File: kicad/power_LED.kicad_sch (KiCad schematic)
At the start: 2 parts

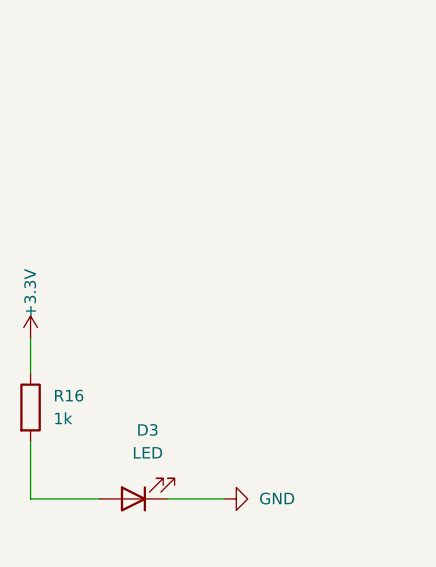
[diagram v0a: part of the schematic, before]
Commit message: feat: remake power management and use the same as the reference DK
Signed-off-by: Bobo Bäck Engström <bobo@id8-engineering.io>
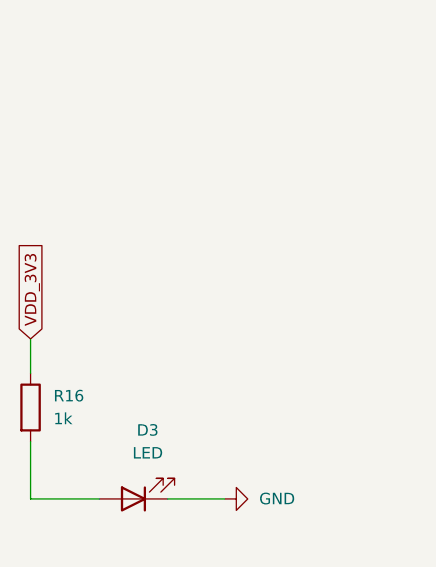
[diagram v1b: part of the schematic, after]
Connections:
- net +3.3V renamed VDD_3V3
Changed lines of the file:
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@@
 		)
 	)
-	(symbol
-		(lib_id "seven_lib:+3V3")
-		(at 87.63 87.63 0)
-		(unit 1)
-		(exclude_from_sim no)
-		(in_bom yes)
-		(on_board yes)
-		(dnp no)
-		(property "Reference" "#PWR044"
-			(at 87.63 91.44 0)
+	(global_label "VDD_3V3"
+		(shape input)
+		(at 87.63 87.63 90)
+		(fields_autoplaced yes)
+		(effects
+			(font
+				(size 1.27 1.27)
+			)
+			(justify left)
+		)
+		(property "Intersheetrefs" "${INTERSHEET_REFS}"
+			(at 87.63 76.541 90)
 			(effects
 				(font
 					(size 1.27 1.27)
 				)
+				(justify left)
 				(hide yes)
 			)
 		)
-		(property "Value" "+3.3V"
-			(at 87.63 82.55 90)
-			(effects
-				(font
-					(size 1.27 1.27)
-				)
-			)
-		)
-		(property "Footprint" ""
-			(at 87.63 87.63 0)
-			(effects
-				(font
-					(size 1.27 1.27)
-				)
-				(hide yes)
-			)
-		)
-		(property "Datasheet" ""
-			(at 87.63 87.63 0)
-			(effects
-				(font
-					(size 1.27 1.27)
-				)
-				(hide yes)
-			)
-		)
-		(property "Description" "Power symbol creates a global label with name \"+3V3\""
-			(at 87.63 87.63 0)
-			(effects
-				(font
-					(size 1.27 1.27)
-				)
-				(hide yes)
-			)
-		)
-		(pin "1"
-		)
-		(instances
-			(project "seven"
-				(path "/8e3cc843-5797-49f3-8b3a-1c11450ccd1e/184102d6-38c7-410c-9d7f-e631dd7f9fe2"
-					(reference "#PWR044")
-					(unit 1)
-				)
-			)
-		)

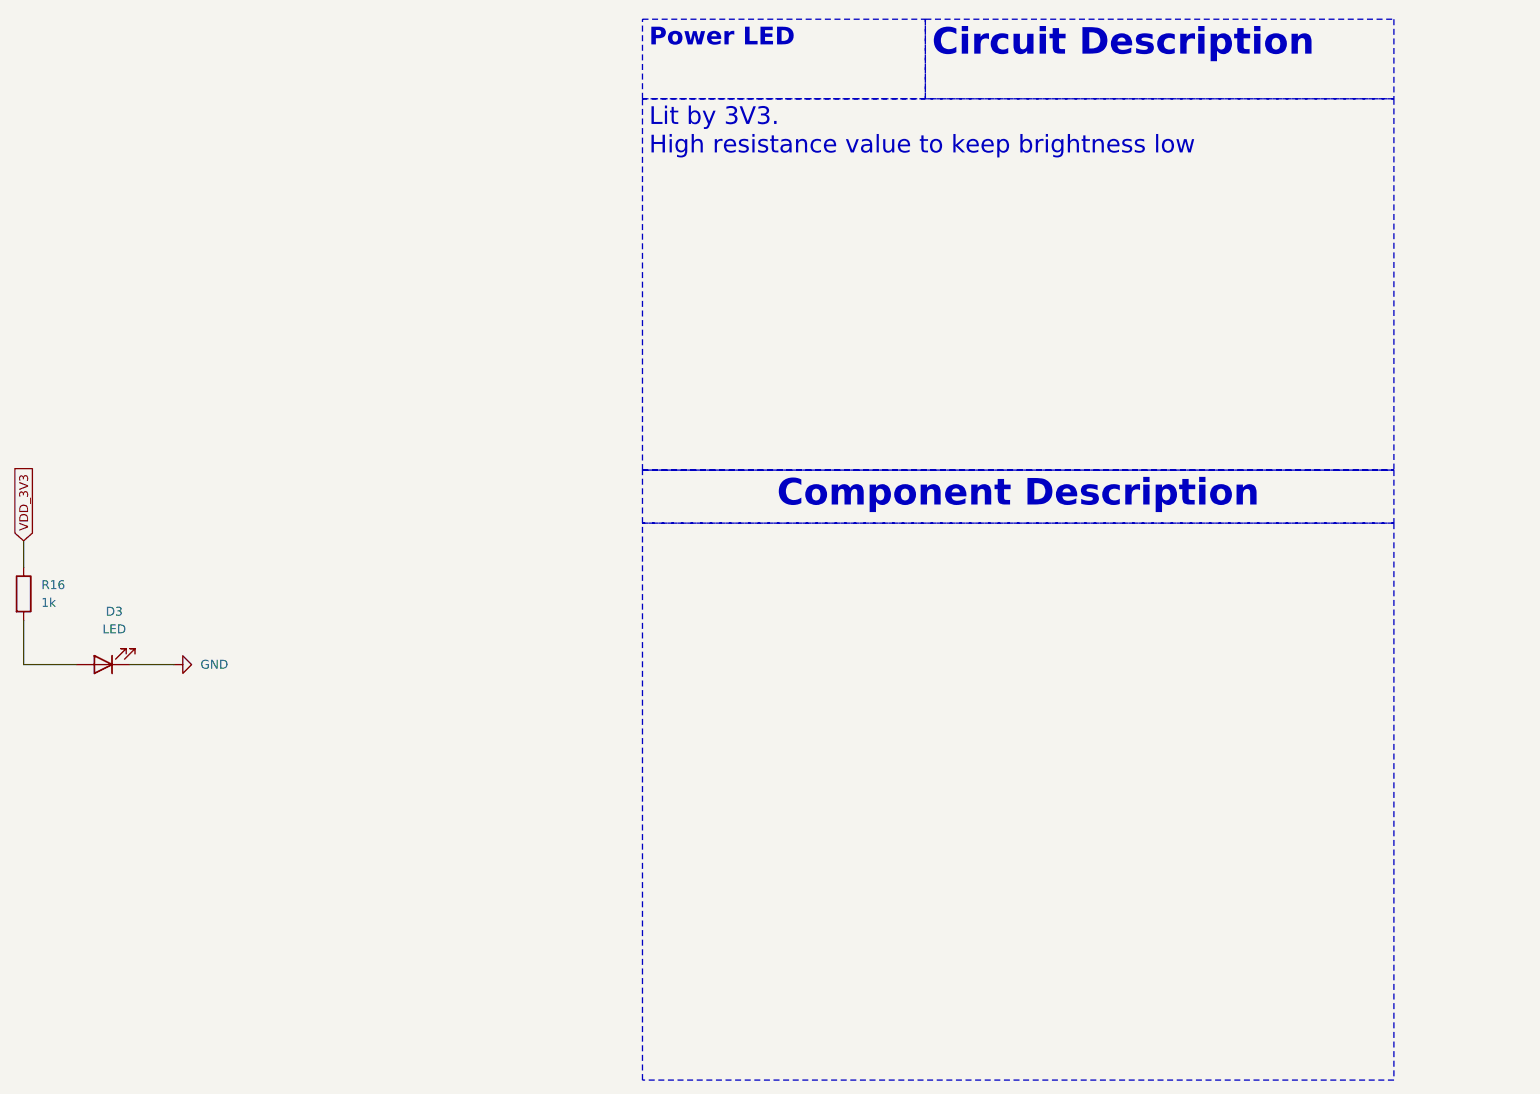
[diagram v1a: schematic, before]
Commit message: docs: update documentation to be more accurate
Signed-off-by: Bobo Bäck Engström <bobo@id8-engineering.io>
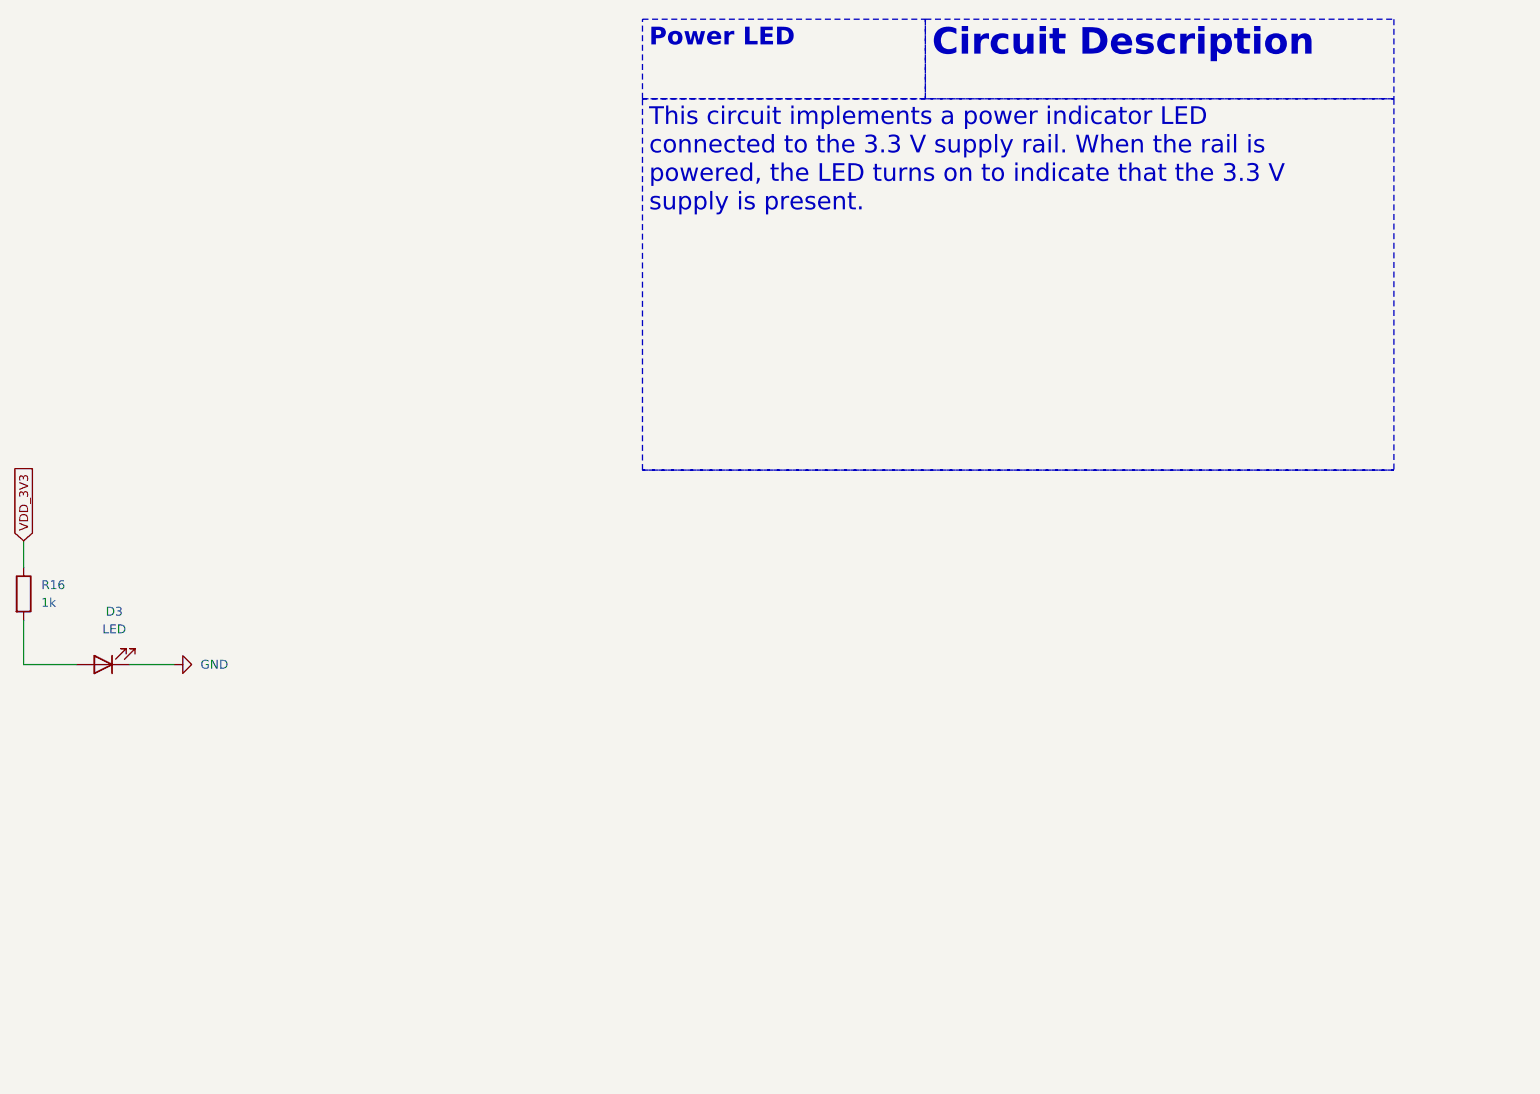
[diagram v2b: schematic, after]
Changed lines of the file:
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@@
-		)
-	)
-	(text_box ""
-		(exclude_from_sim no)
-		(at 176.53 85.09 0)
-		(size 107.95 80.01)
-		(margins 0.9525 0.9525 0.9525 0.9525)
-		(stroke
-			(width 0)
-			(type dash)
-		)
-		(fill
-			(type none)
-		)
-		(effects
-			(font
-				(size 2.54 2.54)
-			)
-			(justify left top)
-		)
-	)
-	(text_box "Component Description\n"
-		(exclude_from_sim no)
-		(at 176.53 77.47 0)
-		(size 107.95 7.62)
-		(margins 0.9525 0.9525 0.9525 0.9525)
-		(stroke
-			(width 0)
-			(type dash)
-		)
-		(fill
-			(type none)
-		)
-		(effects
-			(font
-				(size 3.81 3.81)
-				(thickness 0.762)
-				(bold yes)
-			)
-			(justify top)
 		)
 	)
@@
 		)
 	)
-	(text_box "Lit by 3V3.\nHigh resistance value to keep brightness low"
+	(text_box "This circuit implements a power indicator LED connected to the 3.3 V supply rail. When the rail is powered, the LED turns on to indicate that the 3.3 V supply is present."
 		(exclude_from_sim no)
 		(at 176.53 24.13 0)

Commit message: fix: change R fp to a smaller one
Signed-off-by: Bobo Bäck Engström <bobo@id8-engineering.io>
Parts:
- R16: footprint seven-lib:R_0603_1608Metric -> seven-lib:R_0402_1005Metric
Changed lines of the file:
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@@
 			)
 		)
-		(property "Footprint" "seven-lib:R_0603_1608Metric"
+		(property "Footprint" "seven-lib:R_0402_1005Metric"
 			(at 85.852 95.25 90)
 			(effects

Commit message: feat(PCB): set component-placement example on PCB
This pr will fail due to DRC, skip this and lets have a conversation
about the placement only

Signed-off-by: Bobo Bäck Engström <bobo@id8-engineering.io>
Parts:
- D3: MPN (none) -> TLMG1100-GS08
- R16: MPN (none) -> RC0402FR-071KL
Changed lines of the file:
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@@
 (kicad_sch
-	(version 20250114)
+	(version 20260306)
 	(generator "eeschema")
-	(generator_version "9.0")
+	(generator_version "10.0")
 	(paper "A4")
 	(text "\n\n"
@@
 		(property "Intersheetrefs" "${INTERSHEET_REFS}"
 			(at 87.63 76.541 90)
+			(hide yes)
+			(show_name no)
+			(do_not_autoplace no)
 			(effects
 				(font
@@
 				)
 				(justify left)
-				(hide yes)
 			)
 		)
@@
 		(at 99.06 105.41 180)
 		(unit 1)
+		(body_style 1)
 		(exclude_from_sim no)
 		(in_bom yes)
 		(on_board yes)
+		(in_pos_files yes)
 		(dnp no)
 		(fields_autoplaced yes)
 		(property "Reference" "D3"
 			(at 100.6475 97.79 0)
+			(show_name no)
+			(do_not_autoplace no)
 			(effects
 				(font
@@
 		(property "Value" "LED"
 			(at 100.6475 100.33 0)
+			(show_name no)
+			(do_not_autoplace no)
 			(effects
 				(font
@@
 		(property "Footprint" "seven-lib:LED_0603_1608Metric"
 			(at 99.06 105.41 0)
-			(effects
-				(font
-					(size 1.27 1.27)
-				)
-				(hide yes)
-			)
-		)
-		(property "Datasheet" "~"
-			(at 99.06 105.41 0)
-			(effects
-				(font
-					(size 1.27 1.27)
-				)
-				(hide yes)
+			(hide yes)
+			(show_name no)
+			(do_not_autoplace no)
+			(effects
+				(font
+					(size 1.27 1.27)
+				)
+			)
+		)
+		(property "Datasheet" "https://www.vishay.com/docs/83173/tlmx1100.pdf"
+			(at 99.06 105.41 0)
+			(hide yes)
+			(show_name no)
+			(do_not_autoplace no)
+			(effects
+				(font
+					(size 1.27 1.27)
+				)
 			)
 		)
 		(property "Description" "Light emitting diode"
 			(at 99.06 105.41 0)
-			(effects
-				(font
-					(size 1.27 1.27)
-				)
-				(hide yes)
+			(hide yes)
+			(show_name no)
+			(do_not_autoplace no)
+			(effects
+				(font
+					(size 1.27 1.27)
+				)
 			)
 		)
 		(property "Sim.Pins" "1=K 2=A"
 			(at 99.06 105.41 0)
-			(effects
-				(font
-					(size 1.27 1.27)
-				)
-				(hide yes)
+			(hide yes)
+			(show_name no)
+			(do_not_autoplace no)
+			(effects
+				(font
+					(size 1.27 1.27)
+				)
+			)
+		)
+		(property "MPN" "TLMG1100-GS08"
+			(at 99.06 105.41 0)
+			(hide yes)
+			(show_name no)
+			(do_not_autoplace no)
+			(effects
+				(font
+					(size 1.27 1.27)
+				)
+			)
+		)
+		(property "Manufacturer Part Number" ""
+			(at 99.06 105.41 0)
+			(hide yes)
+			(show_name no)
+			(do_not_autoplace no)
+			(effects
+				(font
+					(size 1.27 1.27)
+				)
 			)
 		)
@@
 		(at 109.22 105.41 90)
 		(unit 1)
+		(body_style 1)
 		(exclude_from_sim no)
 		(in_bom yes)
 		(on_board yes)
+		(in_pos_files yes)
 		(dnp no)
 		(fields_autoplaced yes)
 		(property "Reference" "#PWR045"
 			(at 115.57 105.41 0)
-			(effects
-				(font
-					(size 1.27 1.27)
-				)
-				(hide yes)
+			(hide yes)
+			(show_name no)
+			(do_not_autoplace no)
+			(effects
+				(font
+					(size 1.27 1.27)
+				)
 			)
 		)
 		(property "Value" "GND"
 			(at 113.03 105.4099 90)
+			(show_name no)
+			(do_not_autoplace no)
 			(effects
 				(font
@@
 		(property "Footprint" ""
 			(at 109.22 105.41 0)
-			(effects
-				(font
-					(size 1.27 1.27)
-				)
-				(hide yes)
+			(hide yes)
+			(show_name no)
+			(do_not_autoplace no)
+			(effects
+				(font
+					(size 1.27 1.27)
+				)
 			)
 		)
 		(property "Datasheet" ""
 			(at 109.22 105.41 0)
-			(effects
-				(font
-					(size 1.27 1.27)
-				)
-				(hide yes)
+			(hide yes)
+			(show_name no)
+			(do_not_autoplace no)
+			(effects
+				(font
+					(size 1.27 1.27)
+				)
 			)
 		)
 		(property "Description" "Power symbol creates a global label with name \"GND\" , ground"
 			(at 109.22 105.41 0)
-			(effects
-				(font
-					(size 1.27 1.27)
-				)
-				(hide yes)
+			(hide yes)
+			(show_name no)
+			(do_not_autoplace no)
+			(effects
+				(font
+					(size 1.27 1.27)
+				)
 			)
 		)
@@
 		(at 87.63 95.25 0)
 		(unit 1)
+		(body_style 1)
 		(exclude_from_sim no)
 		(in_bom yes)
 		(on_board yes)
+		(in_pos_files yes)
 		(dnp no)
 		(fields_autoplaced yes)
 		(property "Reference" "R16"
 			(at 90.17 93.9799 0)
+			(show_name no)
+			(do_not_autoplace no)
 			(effects
 				(font
@@
 		(property "Value" "1k"
 			(at 90.17 96.5199 0)
+			(show_name no)
+			(do_not_autoplace no)
 			(effects
 				(font
@@
 		(property "Footprint" "seven-lib:R_0402_1005Metric"
 			(at 85.852 95.25 90)
-			(effects
-				(font
-					(size 1.27 1.27)
-				)
-				(hide yes)
-			)
-		)
-		(property "Datasheet" "~"
+			(hide yes)
+			(show_name no)
+			(do_not_autoplace no)
+			(effects
+				(font
+					(size 1.27 1.27)
+				)
+			)
+		)
+		(property "Datasheet" ""
 			(at 87.63 95.25 0)
-			(effects
-				(font
-					(size 1.27 1.27)
-				)
-				(hide yes)
+			(hide yes)
+			(show_name no)
+			(do_not_autoplace no)
+			(effects
+				(font
+					(size 1.27 1.27)
+				)
 			)
 		)
 		(property "Description" "Resistor"
 			(at 87.63 95.25 0)
-			(effects
-				(font
-					(size 1.27 1.27)
-				)
-				(hide yes)
-			)
-		)
+			(hide yes)
+			(show_name no)
+			(do_not_autoplace no)
+			(effects
+				(font
+					(size 1.27 1.27)
+				)
+			)
+		)
+		(property "MPN" "RC0402FR-071KL"
+			(at 87.63 95.25 0)
+			(hide yes)
+			(show_name no)
+			(do_not_autoplace no)
+			(effects
+				(font
+					(size 1.27 1.27)
+				)
+			)
+		)
+		(property "Manufacturer Part Number" ""
+			(at 87.63 95.25 0)
+			(hide yes)
+			(show_name no)
+			(do_not_autoplace no)
+			(effects
+				(font
+					(size 1.27 1.27)
+				)
+			)
+		)
